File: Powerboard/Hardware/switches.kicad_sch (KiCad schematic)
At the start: 41 parts, among them IC1 TPS259830ONRGER, J2 FAN, J4 Conn_01x02_Male, J5 Conn_01x08_Male, J6 Conn_01x02_Male, Q1 SSM3K15AMFV,L3F, Q10 SQS141ELNW-T1_GE3, Q7 SQS141ELNW-T1_GE3, Q8 SQS141ELNW-T1_GE3, Q9 SQS141ELNW-T1_GE3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

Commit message: fixed resistor value
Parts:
- C24: MPN (none) -> VKME1301H181MV
- C31: MPN (none) -> UMK212ABJ225KG-T
- Q1: MPN (none) -> SSM3K15AMFV,L3F(T
- R28: value 97.6 -> 97.6k
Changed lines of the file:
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@@
+			)
+		)
+		(property "MPN" "VKME1301H181MV"
+			(at 154.94 108.966 0)
+			(effects
+				(font
+					(size 1.27 1.27)
+				)
+				(hide yes)
 			)
 		)
@@
 			)
 		)
+		(property "MPN" "UMK212ABJ225KG-T"
+			(at 132.842 76.454 0)
+			(effects
+				(font
+					(size 1.27 1.27)
+				)
+				(hide yes)
+			)
+		)
 		(pin "2"
 		)
@@
 			)
 		)
+		(property "MPN" "SSM3K15AMFV,L3F(T"
+			(at 242.316 39.878 0)
+			(effects
+				(font
+					(size 1.27 1.27)
+				)
+				(hide yes)
+			)
+		)
 		(pin "1"
 		)
@@
 			)
 		)
-		(property "Value" "97.6"
+		(property "Value" "97.6k"
 			(at 136.3726 110.1781 0)
 			(effects

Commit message: updated mpn on some caps
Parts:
- C22: MPN (none) -> C1005X7S2A103KT000F
- C27: MPN (none) -> CGA0603X5R226M160JT
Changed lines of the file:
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@@
+			)
+		)
+		(property "MPN" " C1005X7S2A103KT000F"
+			(at 216.662 113.538 0)
+			(effects
+				(font
+					(size 1.27 1.27)
+				)
+				(hide yes)
 			)
 		)
@@
 			(at 131.318 108.966 0)
 			(effects
+				(font
+					(size 1.27 1.27)
+				)
+				(hide yes)
+			)
+		)
+		(property "MPN" "CGA0603X5R226M160JT"
+			(at 131.318 108.966 0)
+			(effects

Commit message: esp32 adc cap was in wrong place
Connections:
- net DepVoltage: now also C27.1; no longer C27.2
- net EFuse_OUT: no longer C27.1
- net GND: now also C26.2, C27.2
- net LogicVoltage: now also C26.1; no longer C26.2
- net at C23.1, J5.4 (Pin_4), Q8.10 (D_6)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: no longer C26.1
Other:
- moved on the sheet: C26, C27
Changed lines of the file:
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@@
 	)
 	(junction
-		(at 131.318 106.426)
-		(diameter 0)
-		(color 0 0 0 0)
-	)
-	(junction
 		(at 134.874 106.426)
 		(diameter 0)
@@
 	)
 	(junction
-		(at 219.202 120.142)
+		(at 134.874 118.872)
 		(diameter 0)
 		(color 0 0 0 0)
 	)
 	(junction
-		(at 152.4 66.548)
+		(at 219.202 120.142)
 		(diameter 0)
 		(color 0 0 0 0)
 	)
 	(junction
-		(at 73.406 35.56)
+		(at 152.4 66.548)
 		(diameter 0)
 		(color 0 0 0 0)
 	)
 	(junction
-		(at 68.326 106.426)
+		(at 73.406 35.56)
 		(diameter 0)
 		(color 0 0 0 0)
 	)
 	(junction
-		(at 69.596 106.426)
+		(at 68.326 106.426)
 		(diameter 0)
 		(color 0 0 0 0)
@@
 	)
 	(junction
+		(at 73.152 118.872)
+		(diameter 0)
+		(color 0 0 0 0)
+	)
+	(junction
 		(at 186.69 116.078)
 		(diameter 0)
@@
 	(wire
 		(pts
-			(xy 24.892 64.262) (xy 27.432 64.262)
+			(xy 131.318 118.872) (xy 134.874 118.872)
 		)
 		(stroke
@@
 	(wire
 		(pts
-			(xy 25.146 54.864) (xy 25.146 52.832)
+			(xy 24.892 64.262) (xy 27.432 64.262)
 		)
 		(stroke
@@
 	(wire
 		(pts
-			(xy 219.202 153.162) (xy 221.996 153.162)
+			(xy 25.146 54.864) (xy 25.146 52.832)
 		)
 		(stroke
@@
 	(wire
 		(pts
-			(xy 75.946 60.96) (xy 78.486 60.96)
+			(xy 219.202 153.162) (xy 221.996 153.162)
 		)
 		(stroke
@@
 	(wire
 		(pts
-			(xy 244.856 24.638) (xy 244.856 23.368)
+			(xy 75.946 60.96) (xy 78.486 60.96)
 		)
 		(stroke
@@
 	(wire
 		(pts
-			(xy 69.596 111.506) (xy 69.596 112.522)
+			(xy 244.856 24.638) (xy 244.856 23.368)
 		)
 		(stroke
@@
 	(wire
 		(pts
-			(xy 68.326 106.426) (xy 69.596 106.426)
+			(xy 68.326 106.426) (xy 73.152 106.426)
 		)
 		(stroke
@@
 	(wire
 		(pts
-			(xy 131.318 111.506) (xy 131.318 112.776)
-		)
-		(stroke
-			(width 0)
-			(type default)
-		)
-	)
-	(wire
-		(pts
 			(xy 134.874 111.506) (xy 134.874 112.776)
 		)
@@
 	(wire
 		(pts
+			(xy 69.596 117.602) (xy 69.596 118.872)
+		)
+		(stroke
+			(width 0)
+			(type default)
+		)
+	)
+	(wire
+		(pts
 			(xy 91.186 106.426) (xy 73.152 106.426)
 		)
@@
 	(wire
 		(pts
-			(xy 131.318 106.426) (xy 114.554 106.426)
+			(xy 114.554 106.426) (xy 134.874 106.426)
 		)
 		(stroke
@@
 	(wire
 		(pts
-			(xy 64.77 112.522) (xy 69.596 112.522)
-		)
-		(stroke
-			(width 0)
-			(type default)
-		)
-	)
-	(wire
-		(pts
 			(xy 216.916 28.702) (xy 216.916 31.75)
 		)
@@
 	(wire
 		(pts
-			(xy 69.596 106.426) (xy 73.152 106.426)
-		)
-		(stroke
-			(width 0)
-			(type default)
-		)
-	)
-	(wire
-		(pts
 			(xy 123.698 91.948) (xy 138.43 91.948)
 		)
@@
 	(wire
 		(pts
+			(xy 69.596 118.872) (xy 73.152 118.872)
+		)
+		(stroke
+			(width 0)
+			(type default)
+		)
+	)
+	(wire
+		(pts
 			(xy 103.886 128.27) (xy 108.204 128.27)
 		)
@@
 	(wire
 		(pts
+			(xy 131.318 117.856) (xy 131.318 118.872)
+		)
+		(stroke
+			(width 0)
+			(type default)
+		)
+	)
+	(wire
+		(pts
 			(xy 162.56 62.992) (xy 164.846 62.992)
 		)
@@
 	(wire
 		(pts
+			(xy 59.944 112.522) (xy 69.596 112.522)
+		)
+		(stroke
+			(width 0)
+			(type default)
+		)
+	)
+	(wire
+		(pts
 			(xy 68.326 90.678) (xy 68.326 93.218)
 		)
@@
 	(wire
 		(pts
-			(xy 134.874 106.426) (xy 131.318 106.426)
-		)
-		(stroke
-			(width 0)
-			(type default)
-		)
-	)
-	(wire
-		(pts
 			(xy 134.874 112.776) (xy 139.192 112.776)
 		)
@@
 	(hierarchical_label "LogicVoltage"
 		(shape output)
-		(at 64.77 112.522 270)
+		(at 59.944 112.522 270)
 		(fields_autoplaced yes)
 		(effects
@@
 	(symbol
 		(lib_id "Device:C_Small")
-		(at 69.596 108.966 0)
+		(at 69.596 115.062 0)
 		(unit 1)
 		(exclude_from_sim no)
@@
 		(dnp no)
 		(property "Reference" "C26"
-			(at 62.23 108.0657 0)
+			(at 62.23 114.1617 0)
 			(effects
 				(font
@@
 		)
 		(property "Value" "0.1uF"
-			(at 62.23 110.49 0)
+			(at 62.23 116.586 0)
 			(effects
 				(font
@@
 		)
 		(property "Footprint" "Capacitor_SMD:C_0402_1005Metric"
-			(at 69.596 108.966 0)
+			(at 69.596 115.062 0)
 			(effects
 				(font
@@
 		)
 		(property "Datasheet" "~"
-			(at 69.596 108.966 0)
+			(at 69.596 115.062 0)
 			(effects
 				(font
@@
 		)
 		(property "Description" "Unpolarized capacitor, small symbol"
-			(at 69.596 108.966 0)
+			(at 69.596 115.062 0)
 			(effects
 				(font
@@
 	(symbol
 		(lib_id "Device:C_Small")
-		(at 131.318 108.966 0)
+		(at 131.318 115.316 0)
 		(unit 1)
 		(exclude_from_sim no)
@@
 		(dnp no)
 		(property "Reference" "C27"
-			(at 123.952 108.0657 0)
+			(at 126.238 117.4637 0)
 			(effects
 				(font
@@
 		)
 		(property "Value" "0.1uF"
-			(at 123.952 110.49 0)
+			(at 126.238 119.888 0)
 			(effects
 				(font
@@
 		)
 		(property "Footprint" "Capacitor_SMD:C_0402_1005Metric"
-			(at 131.318 108.966 0)
+			(at 131.318 115.316 0)
 			(effects
 				(font
@@
 		)
 		(property "Datasheet" "~"
-			(at 131.318 108.966 0)
+			(at 131.318 115.316 0)
 			(effects
 				(font
@@
 		)
 		(property "Description" "Unpolarized capacitor, small symbol"
-			(at 131.318 108.966 0)
+			(at 131.318 115.316 0)
 			(effects
 				(font
@@
 		)
 		(property "MPN" "CGA0603X5R226M160JT"
-			(at 131.318 108.966 0)
+			(at 131.318 115.316 0)
 			(effects
 				(font

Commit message: post Andrei review
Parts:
- removed C29: 2.2uF, Capacitor_SMD:C_0402_1005Metric, symbol Device:C_Small
- removed C31: 2.2uF, Capacitor_SMD:C_0805_2012Metric, symbol Device:C_Small
- removed R44, R45: 100k, Resistor_SMD:R_0402_1005Metric, symbol Device:R_Small
- added D4: SMCJ24AHE3_A/H, Diode_SMD:D_SMC, symbol Diode:PTVS5V0Z1USK
- R42: value 681 -> 680
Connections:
- net EFuse_IN: now also D4.1 (K)
- net GND: now also D4.2 (A)

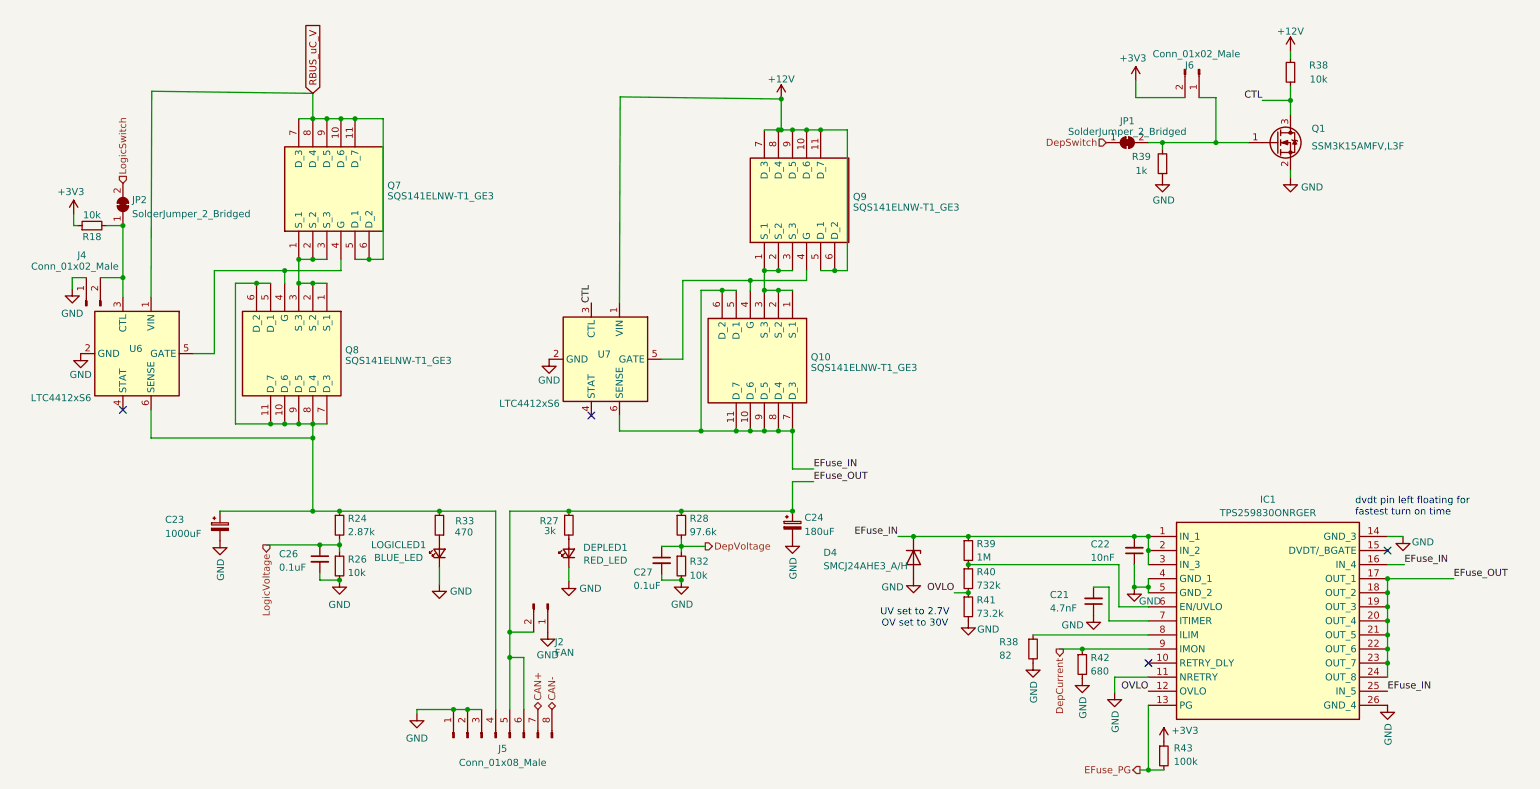
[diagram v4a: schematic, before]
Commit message: moved efuse upstream of ltc
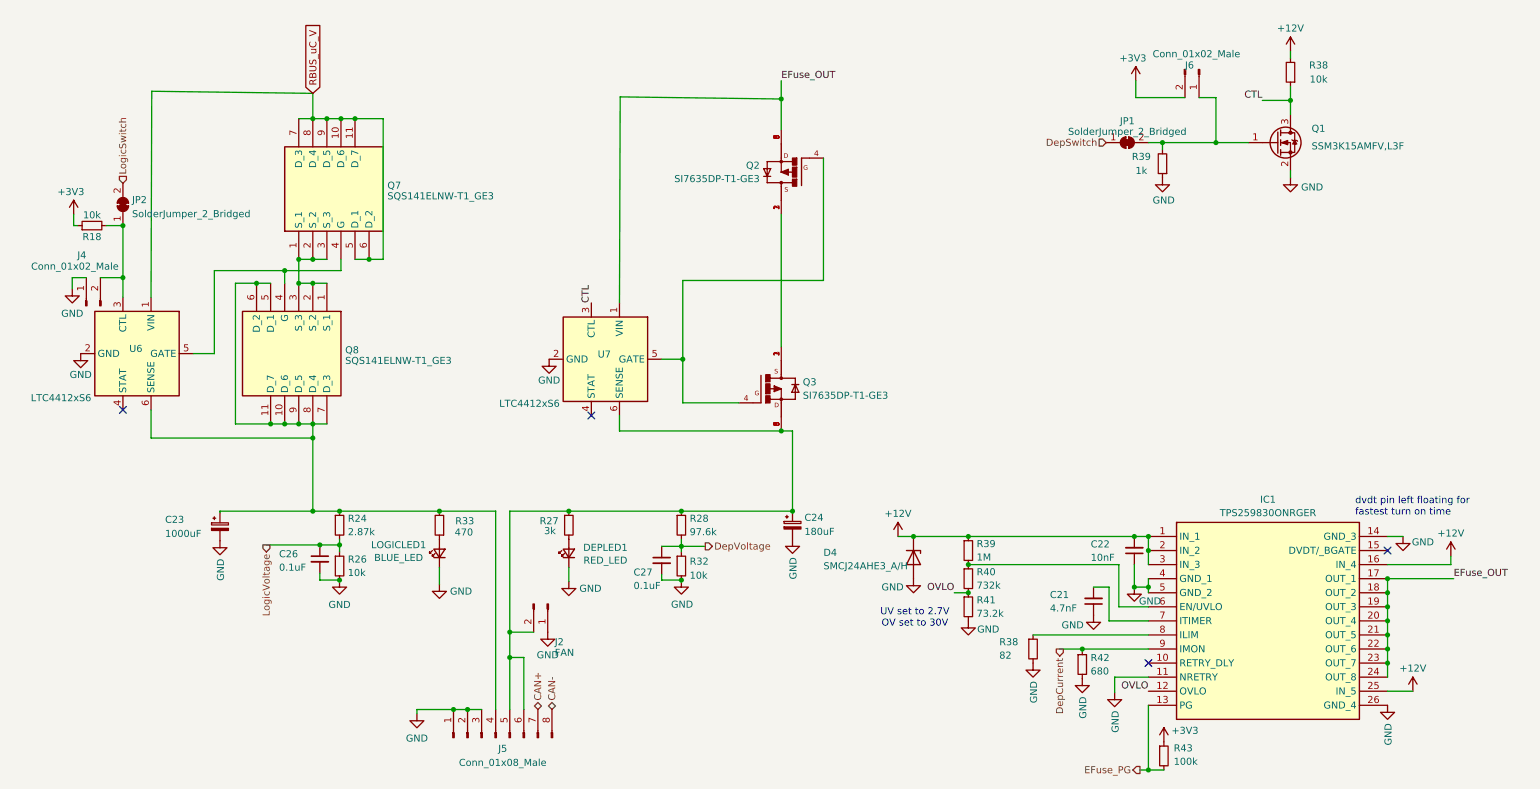
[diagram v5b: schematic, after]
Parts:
- removed Q10, Q9: SQS141ELNW-T1_GE3, iclr:SQS850ENT1_GE3, symbol iclr:SQS141ELNW-T1_GE3
- added Q2, Q3: SI7635DP-T1-GE3, Package_SO:PowerPAK_SO-8_Single, symbol iclr:SI7635DP-T1-GE3
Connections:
- net +12V: now also C22.2, D4.1 (K), IC1.1 (IN_1), IC1.16 (IN_4), IC1.2 (IN_2), IC1.25 (IN_5), IC1.3 (IN_3), R39.1; no longer U7.1 (VIN)
- net EFuse_OUT: now also U7.1 (VIN), Q2.5, Q2.6, Q2.7, Q2.8, Q2.9; no longer C24.1, J2.2 (Pin_2), J5.5 (Pin_5), J5.6 (Pin_6), R27.1, R28.1
- net at U7.5 (GATE): now also Q2.4, Q3.4
- removed net EFuse_IN: C22.2, D4.1 (K), IC1.1 (IN_1), IC1.16 (IN_4), IC1.2 (IN_2), IC1.25 (IN_5), IC1.3 (IN_3), R39.1, U7.6 (SENSE)
- new net: C24.1, J2.2 (Pin_2), J5.5 (Pin_5), J5.6 (Pin_6), Q3.5, Q3.6, Q3.7, Q3.8, Q3.9, R27.1, R28.1, U7.6 (SENSE)
- new net: Q2.1, Q2.2, Q2.3, Q3.1, Q3.2, Q3.3
